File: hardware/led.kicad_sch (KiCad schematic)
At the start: 2 parts

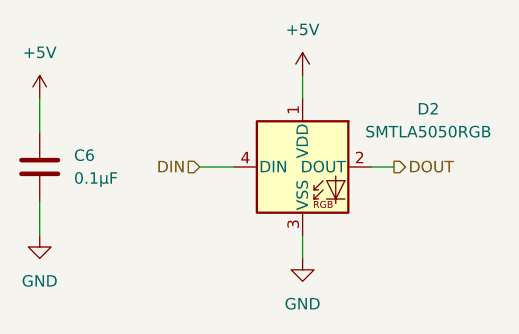
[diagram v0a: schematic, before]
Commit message: Address schematic audit findings
- Move C15 to the ESP32 EN node for proper power-on RC delay and button reset
- Add 10k boot-glitch pull-downs (R13-R16) on the CD4504 level shifter inputs
- Add NCH8200HV input capacitor (C16)
- Switch D2-D4 to the Bivar SMTLA5050RGB symbol/footprint
- Label nixie anode nets and add HV net class with custom DRC clearance rules
- Normalize value formats and assign missing footprints
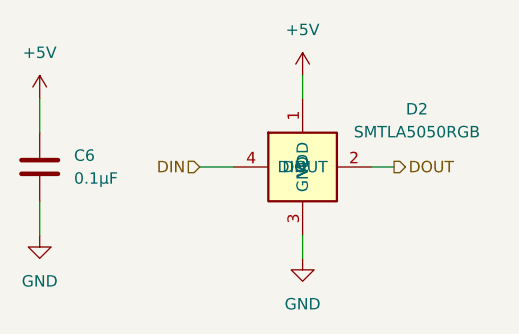
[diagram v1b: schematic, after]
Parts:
- D2: footprint LED_SMD:LED_WS2812B_PLCC4_5.0x5.0mm_P3.2mm -> nixie-esp32:SMTLA5050RGB; symbol LED:WS2812B -> nixie-esp32:SMTLA5050RGB; Manufacturer (none) -> Bivar; Manufacturer_Part_Number (none) -> SMTLA5050RGB
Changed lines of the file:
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@@
 	)
 	(symbol
-		(lib_id "LED:WS2812B")
+		(lib_id "nixie-esp32:SMTLA5050RGB")
 		(at 143.51 85.09 0)
 		(unit 1)
@@
 		(fields_autoplaced yes)
 		(property "Reference" "D2"
-			(at 157.48 78.6698 0)
+			(at 156.21 78.6698 0)
 			(show_name no)
 			(do_not_autoplace no)
@@
 		)
 		(property "Value" "SMTLA5050RGB"
-			(at 157.48 81.2098 0)
+			(at 156.21 81.2098 0)
 			(show_name no)
 			(do_not_autoplace no)
@@
 			)
 		)
-		(property "Footprint" "LED_SMD:LED_WS2812B_PLCC4_5.0x5.0mm_P3.2mm"
-			(at 144.78 92.71 0)
+		(property "Footprint" "nixie-esp32:SMTLA5050RGB"
+			(at 148.59 92.71 0)
 			(hide yes)
 			(show_name no)
@@
 					(size 1.27 1.27)
 				)
-				(justify left top)
 			)
 		)
-		(property "Datasheet" "https://cdn-shop.adafruit.com/datasheets/WS2812B.pdf"
-			(at 146.05 94.615 0)
+		(property "Datasheet" "${KIPRJMOD}/../datasheets/SMTLA5050RGB.pdf"
+			(at 148.59 95.25 0)
 			(hide yes)
 			(show_name no)
@@
 					(size 1.27 1.27)
 				)
-				(justify left top)
 			)
 		)
-		(property "Description" "RGB LED with integrated controller"
-			(at 143.51 85.09 0)
+		(property "Description" "Bivar SMTLA5050RGB addressable RGB LED, 5.0 x 5.4 x 1.6 mm, single-wire cascade, 3.5-7.5 V supply"
+			(at 148.59 97.79 0)
 			(hide yes)
 			(show_name no)
+			(do_not_autoplace no)
+			(effects
+				(font
+					(size 1.27 1.27)
+				)
+			)
+		)
+		(property "Manufacturer" "Bivar"
+			(at 148.59 100.33 0)
+			(hide yes)
+			(show_name no)
+			(do_not_autoplace no)
+			(effects
+				(font
+					(size 1.27 1.27)
+				)
+			)
+		)
+		(property "Manufacturer_Part_Number" "SMTLA5050RGB"
+			(at 148.59 102.87 0)
+			(hide yes)
+			(show_name no)
